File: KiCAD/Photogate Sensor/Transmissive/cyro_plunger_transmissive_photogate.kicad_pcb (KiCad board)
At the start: 2 copper layers, 122 x 70 mm, 46 parts, among them J2 FFC Socket, J3 USB_B_Micro, J4 UPDI socket, J6 Conn_01x03_Socket, Q1 Q_NMOS_GSD, Q2 Q_NMOS_GSD, Q3 Q_NMOS_GSD, Q4 Q_NMOS_GSD, U1 5V LDO, U2 Opamp_Dual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

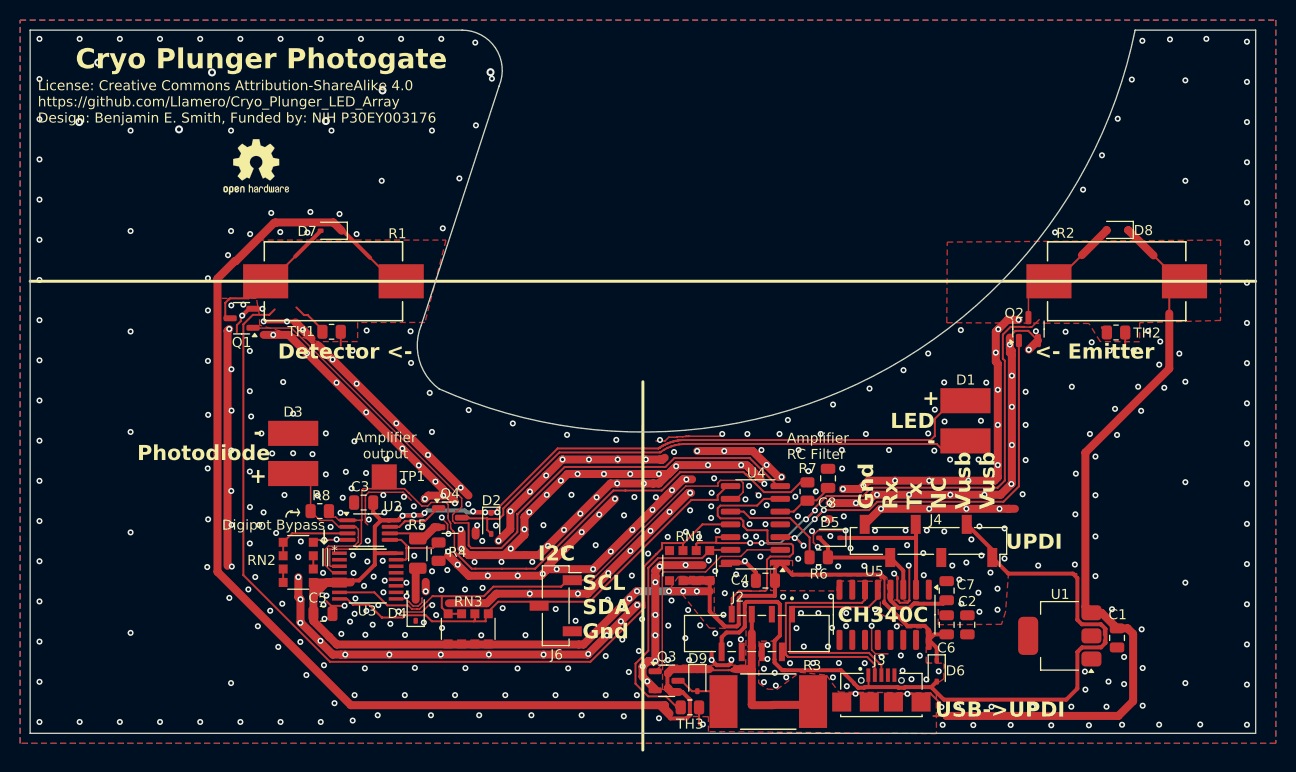
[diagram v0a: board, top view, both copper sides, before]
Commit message: Thermally isolated heaters
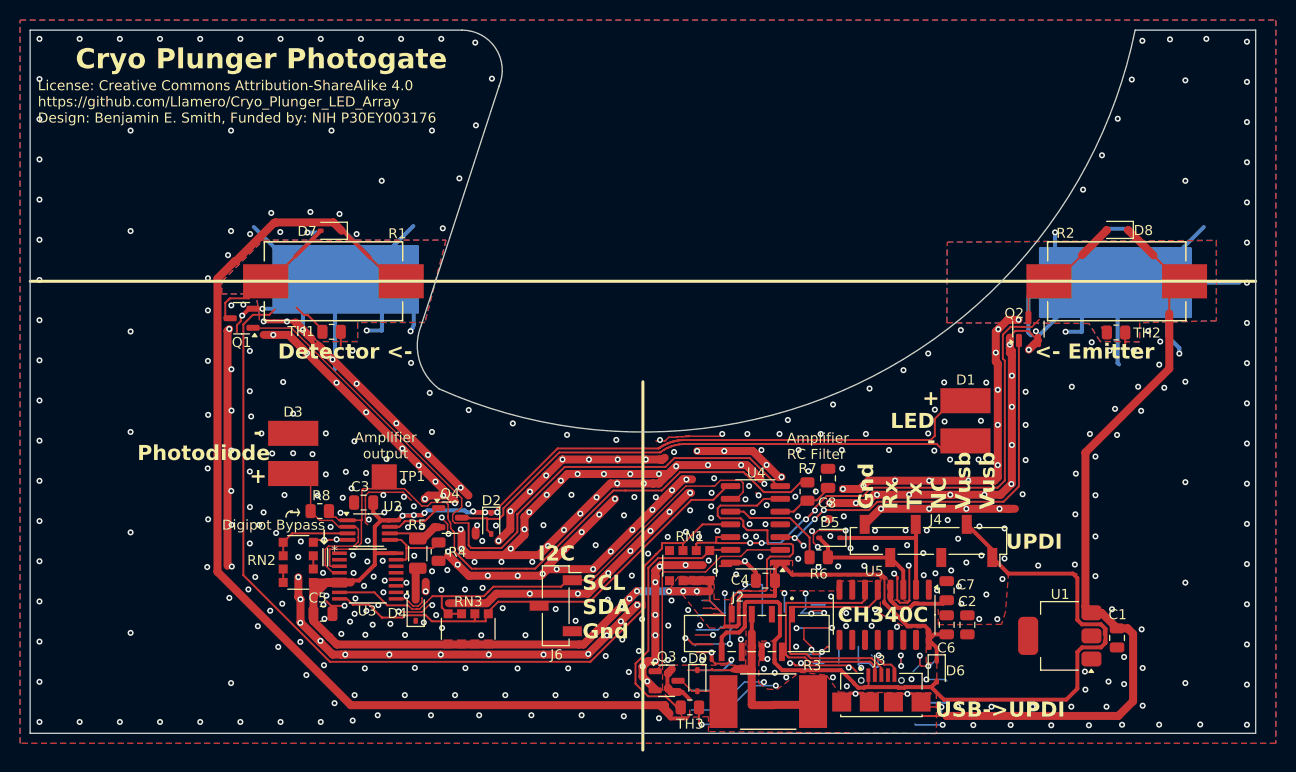
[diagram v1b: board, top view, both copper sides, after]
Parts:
- removed SYM3: Logo_Open_Hardware_Small, Symbol:OSHW-Logo2_7.3x6mm_SilkScreen
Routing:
- net GND: track 462.8 -> 764.4 mm, vias 578 -> 573
- net +5V: track 186.0 -> 190.0 mm
- net +12V: track 215.8 -> 214.2 mm
- added copper zone on B.Cu, net /Therm1
- added copper zone on B.Cu, net /Therm2

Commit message: connection board wired and skew matched
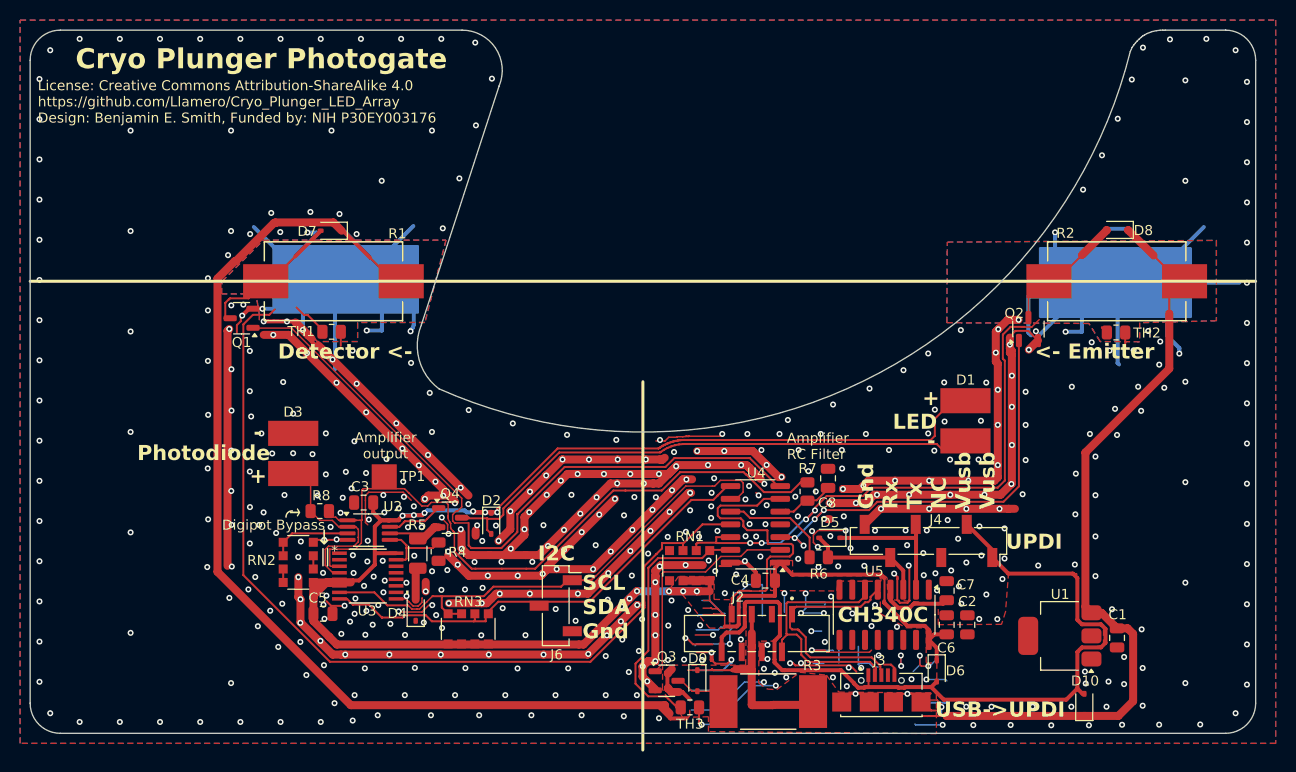
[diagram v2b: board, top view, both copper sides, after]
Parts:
- added D10: D_Schottky, Diode_SMD:D_SOD-323, F.Cu at (204.9, 167.1)
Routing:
- net GND: track 764.4 -> 760.2 mm
- net /D+: track 25.3 -> 23.8 mm
- net /Vusb: track 80.0 -> 80.9 mm
- net /D-: track 25.2 -> 25.7 mm
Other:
- outline, holes or cut-outs redrawn

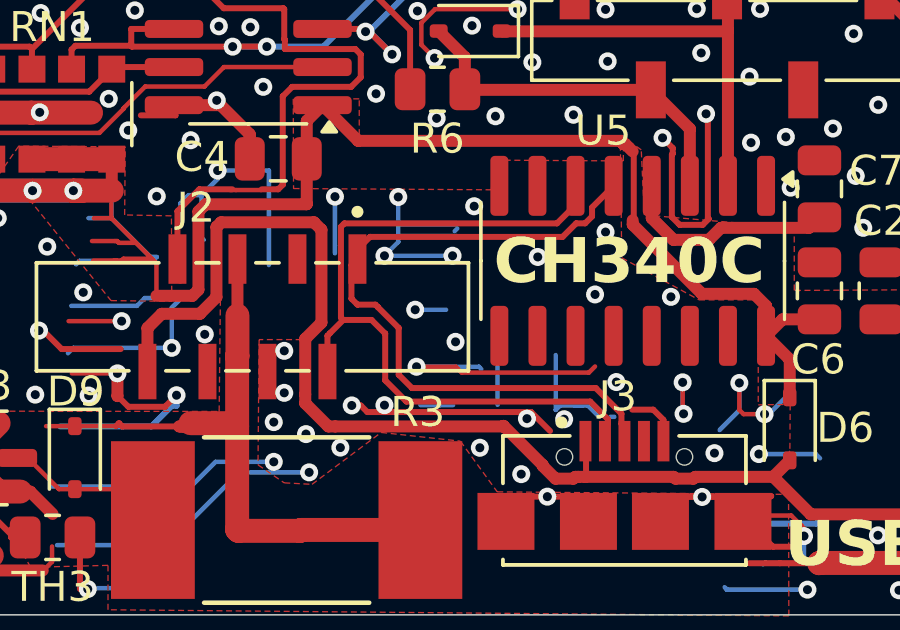
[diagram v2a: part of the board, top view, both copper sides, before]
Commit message: Skew matched and impedance approx. 90 ohm on photogate board
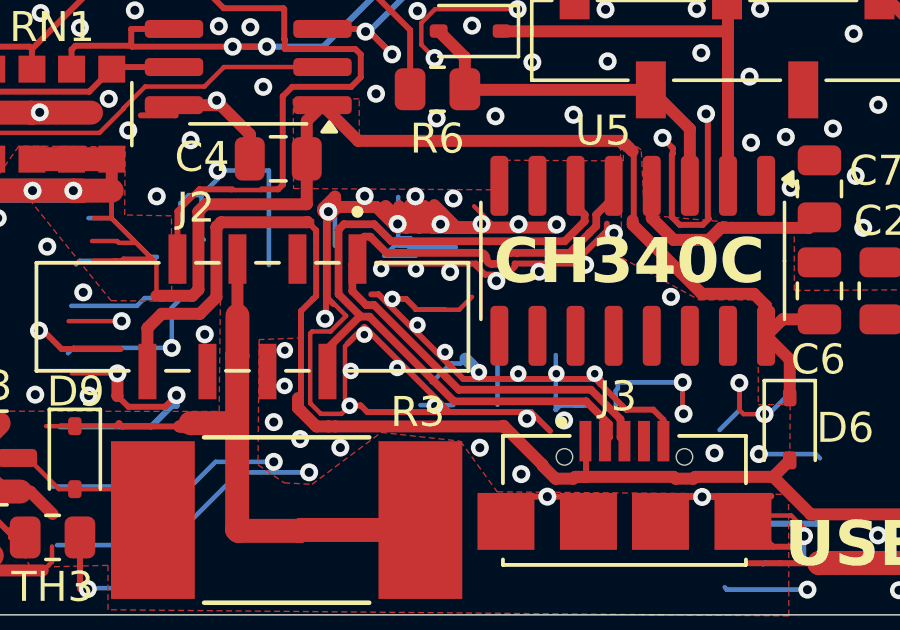
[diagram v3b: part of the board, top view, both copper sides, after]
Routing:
- net GND: track 760.2 -> 822.8 mm, vias 573 -> 588
